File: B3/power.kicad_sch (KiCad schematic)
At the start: 31 parts, among them U301 74HC04, U302 74HC125, U303 74HC74, U304 74HC74, U305 74HC74, U306 74HC32, U309 74HC00, U314 74HC32, U316 74HC00, U317 74HC74, U318 74HC08, U319 74HC32

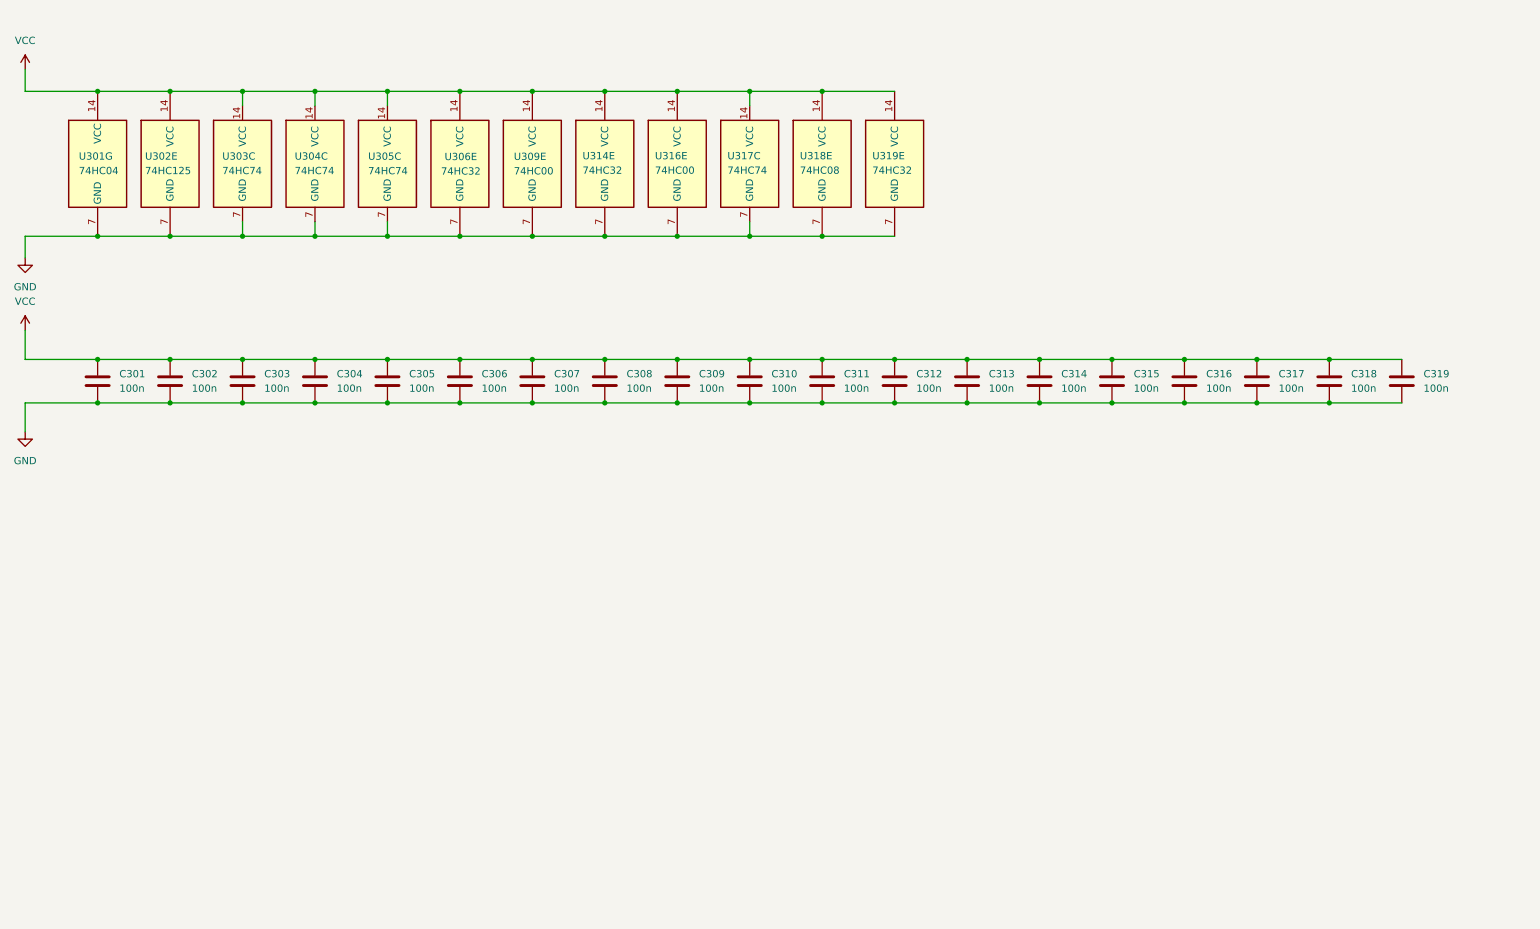
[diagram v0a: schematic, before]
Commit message: B3 added. First revision
Still not verified.
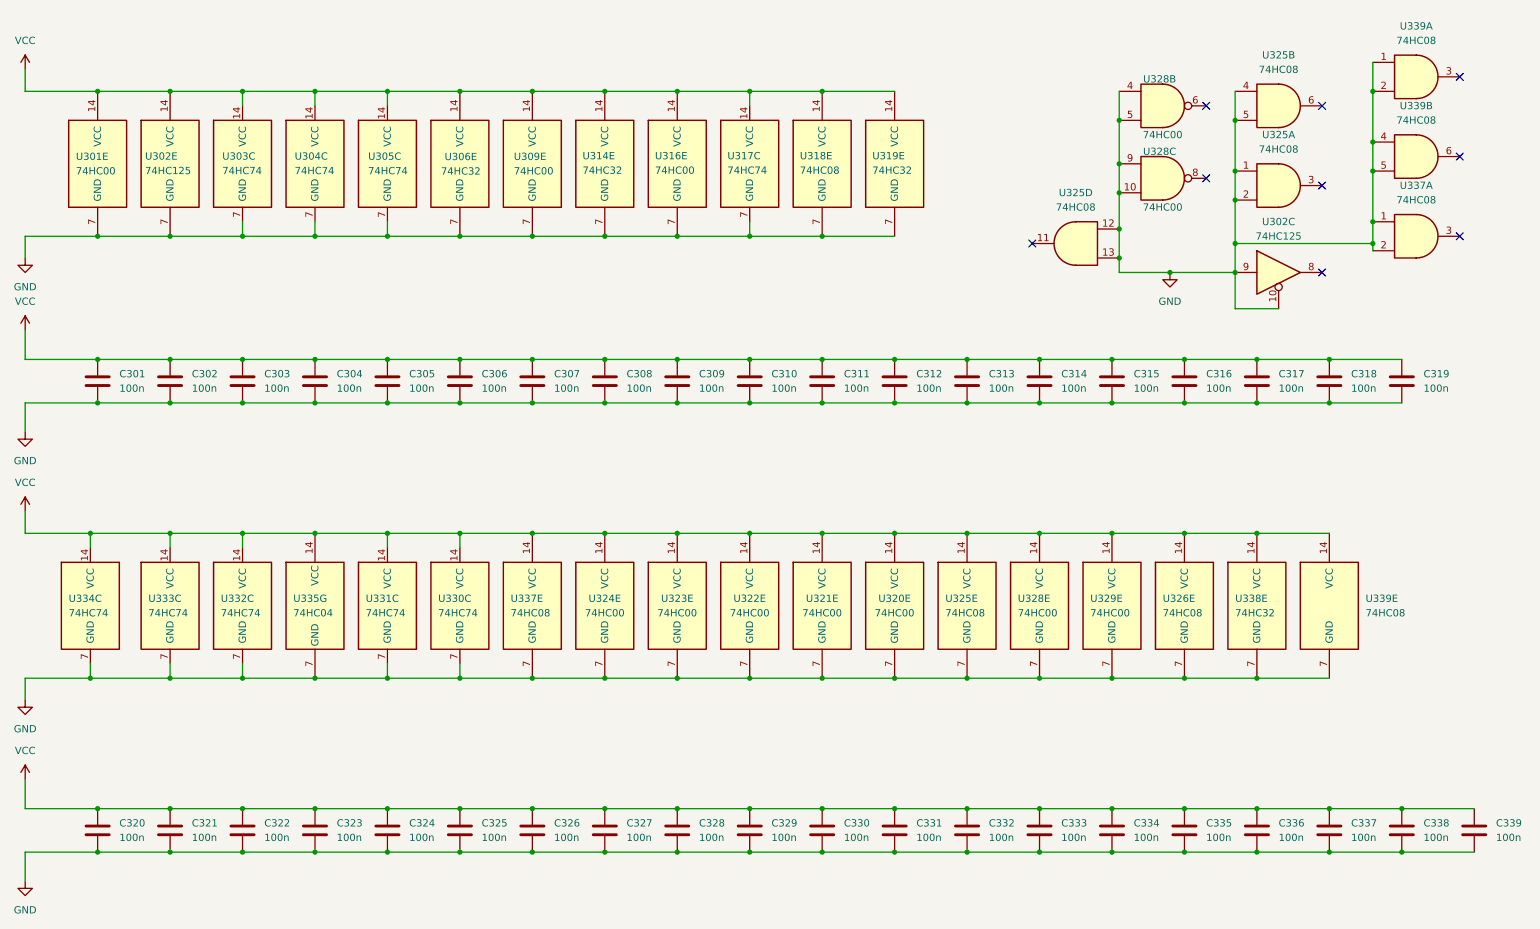
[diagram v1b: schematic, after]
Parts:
- removed U301: 74HC04, Package_SO:SO-14_3.9x8.65mm_P1.27mm, symbol 74xx:74HC04
- added C320, C321, C322, C323, C324, C325, C326, C327, C328, C329, C330, C331, C332, C333, C334, C335, C336, C337, C338, C339: 100n, Capacitor_SMD:C_0603_1608Metric, symbol Device:C
- added U301, U320, U321, U322, U323, U324, U328, U329: 74HC00, Package_SO:SO-14_3.9x8.65mm_P1.27mm, symbol 74xx:74HC00
- added unit 3 of U302
- added U325, U326, U337, U339: 74HC08, Package_SO:SO-14_3.9x8.65mm_P1.27mm, symbol Custom 74xx:74HC08
- added U330, U331, U332, U333, U334: 74HC74, Package_SO:SO-14_3.9x8.65mm_P1.27mm, symbol 74xx:74HC74
- added U335: 74HC04, Package_SO:SO-14_3.9x8.65mm_P1.27mm, symbol 74xx:74HC04
- added U338: 74HC32, Package_SO:SO-14_3.9x8.65mm_P1.27mm, symbol 74xx:74LS32
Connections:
- net GND: now also C320.2, C321.2, C322.2, C323.2, C324.2, C325.2, C326.2, C327.2, C328.2, C329.2, C330.2, C331.2, C332.2, C333.2, C334.2, C335.2, C336.2, C337.2, C338.2, C339.2, U301.7 (GND), U302.10, U302.9, U320.7 (GND), U321.7 (GND), U322.7 (GND), U323.7 (GND), U324.7 (GND), U325.1, U325.12, U325.13, U325.2, U325.4, U325.5, U325.7 (GND), U326.7 (GND), U328.10, U328.4, U328.5, U328.7 (GND), U328.9, U329.7 (GND), U330.7 (GND), U331.7 (GND), U332.7 (GND), U333.7 (GND), U334.7 (GND), U335.7 (GND), U337.1, U337.2, U337.7 (GND), U338.7 (GND), U339.1, U339.2, U339.4, U339.5, U339.7 (GND)
- net VCC: now also C320.1, C321.1, C322.1, C323.1, C324.1, C325.1, C326.1, C327.1, C328.1, C329.1, C330.1, C331.1, C332.1, C333.1, C334.1, C335.1, C336.1, C337.1, C338.1, C339.1, U301.14 (VCC), U320.14 (VCC), U321.14 (VCC), U322.14 (VCC), U323.14 (VCC), U324.14 (VCC), U325.14 (VCC), U326.14 (VCC), U328.14 (VCC), U329.14 (VCC), U330.14 (VCC), U331.14 (VCC), U332.14 (VCC), U333.14 (VCC), U334.14 (VCC), U335.14 (VCC), U337.14 (VCC), U338.14 (VCC), U339.14 (VCC)
- no-connect marks 0 -> 9

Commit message: .
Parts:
- removed unit 1 of U325
- removed unit 3 of U328
- added unit 3 of U309
- added unit 4 of U316
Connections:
- net GND: now also U309.10, U309.9, U316.12, U316.13
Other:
- company: (none) -> Daniel Molina
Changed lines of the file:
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@@
   (title_block
     (title "74HCT6526 Board 3")
-    (date "2022-09-11")
-    (rev "0.1")
+    (date "2022-10-08")
+    (rev "0.1.2")
+    (company "Daniel Molina")
+    (comment 1 "https://github.com/dmolinagarcia/74HCT6526")
   )
   (junction (at 160.02 152.4) (diameter 0) (color 0 0 0 0)
@@
   (junction (at 96.52 52.07) (diameter 0) (color 0 0 0 0)
   )
-  (junction (at 232.41 45.72) (diameter 0) (color 0 0 0 0)
-  )
   (junction (at 256.54 40.64) (diameter 0) (color 0 0 0 0)
   )
@@
   (junction (at 185.42 73.66) (diameter 0) (color 0 0 0 0)
   )
-  (junction (at 232.41 40.64) (diameter 0) (color 0 0 0 0)
-  )
   (junction (at 83.82 52.07) (diameter 0) (color 0 0 0 0)
   )
@@
   (junction (at 223.52 81.28) (diameter 0) (color 0 0 0 0)
   )
-  (junction (at 212.09 39.37) (diameter 0) (color 0 0 0 0)
-  )
   (junction (at 134.62 152.4) (diameter 0) (color 0 0 0 0)
   )
@@
   (junction (at 121.92 73.66) (diameter 0) (color 0 0 0 0)
   )
+  (junction (at 232.41 39.37) (diameter 0) (color 0 0 0 0)
+  )
   (junction (at 198.12 129.54) (diameter 0) (color 0 0 0 0)
   )
@@
   (junction (at 121.92 152.4) (diameter 0) (color 0 0 0 0)
   )
+  (junction (at 212.09 42.545) (diameter 0) (color 0 0 0 0)
+  )
   (junction (at 121.92 81.28) (diameter 0) (color 0 0 0 0)
   )
@@
   (junction (at 71.12 26.67) (diameter 0) (color 0 0 0 0)
   )
-  (junction (at 212.09 44.45) (diameter 0) (color 0 0 0 0)
-  )
   (junction (at 58.42 81.28) (diameter 0) (color 0 0 0 0)
   )
@@
   (junction (at 160.02 104.14) (diameter 0) (color 0 0 0 0)
   )
+  (junction (at 232.41 44.45) (diameter 0) (color 0 0 0 0)
+  )
   (junction (at 185.42 104.14) (diameter 0) (color 0 0 0 0)
   )
@@
   )
   (junction (at 185.42 160.02) (diameter 0) (color 0 0 0 0)
+  )
+  (junction (at 212.09 47.625) (diameter 0) (color 0 0 0 0)
   )
   (junction (at 160.02 52.07) (diameter 0) (color 0 0 0 0)
@@
   (no_connect (at 247.65 58.42))
   (no_connect (at 247.65 29.21))
-  (no_connect (at 227.33 41.91))
+  (no_connect (at 247.65 41.91))
+  (no_connect (at 227.33 45.085))
   (no_connect (at 196.85 53.34))
   (no_connect (at 227.33 29.21))
-  (no_connect (at 247.65 43.18))
   (no_connect (at 271.78 52.07))
   (no_connect (at 271.78 38.1))
@@
     (stroke (width 0) (type default) (color 0 0 0 0))
   )
-  (wire (pts (xy 212.09 31.75) (xy 212.09 39.37))
-    (stroke (width 0) (type default) (color 0 0 0 0))
-  )
   (wire (pts (xy 160.02 52.07) (xy 172.72 52.07))
     (stroke (width 0) (type default) (color 0 0 0 0))
@@
     (stroke (width 0) (type default) (color 0 0 0 0))
   )
+  (wire (pts (xy 212.09 31.75) (xy 212.09 42.545))
+    (stroke (width 0) (type default) (color 0 0 0 0))
+  )
   (wire (pts (xy 109.22 104.14) (xy 121.92 104.14))
     (stroke (width 0) (type default) (color 0 0 0 0))
@@
     (stroke (width 0) (type default) (color 0 0 0 0))
   )
+  (wire (pts (xy 232.41 39.37) (xy 232.41 44.45))
+    (stroke (width 0) (type default) (color 0 0 0 0))
+  )
   (wire (pts (xy 134.62 73.66) (xy 147.32 73.66))
     (stroke (width 0) (type default) (color 0 0 0 0))
@@
     (stroke (width 0) (type default) (color 0 0 0 0))
   )
+  (wire (pts (xy 232.41 44.45) (xy 232.41 53.34))
+    (stroke (width 0) (type default) (color 0 0 0 0))
+  )
   (wire (pts (xy 232.41 53.34) (xy 256.54 53.34))
     (stroke (width 0) (type default) (color 0 0 0 0))
@@
     (stroke (width 0) (type default) (color 0 0 0 0))
   )
-  (wire (pts (xy 232.41 31.75) (xy 232.41 40.64))
-    (stroke (width 0) (type default) (color 0 0 0 0))
-  )
   (wire (pts (xy 147.32 26.67) (xy 147.32 29.21))
     (stroke (width 0) (type default) (color 0 0 0 0))
@@
     (stroke (width 0) (type default) (color 0 0 0 0))
   )
-  (wire (pts (xy 212.09 39.37) (xy 212.09 44.45))
-    (stroke (width 0) (type default) (color 0 0 0 0))
-  )
   (wire (pts (xy 185.42 104.14) (xy 198.12 104.14))
     (stroke (width 0) (type default) (color 0 0 0 0))
   )
-  (wire (pts (xy 232.41 40.64) (xy 232.41 45.72))
-    (stroke (width 0) (type default) (color 0 0 0 0))
-  )
   (wire (pts (xy 212.09 55.88) (xy 212.09 58.42))
     (stroke (width 0) (type default) (color 0 0 0 0))
@@
     (stroke (width 0) (type default) (color 0 0 0 0))
   )
-  (wire (pts (xy 232.41 45.72) (xy 232.41 53.34))
+  (wire (pts (xy 232.41 31.75) (xy 232.41 39.37))
     (stroke (width 0) (type default) (color 0 0 0 0))
   )
@@
     (stroke (width 0) (type default) (color 0 0 0 0))
   )
+  (wire (pts (xy 212.09 47.625) (xy 212.09 50.8))
+    (stroke (width 0) (type default) (color 0 0 0 0))
+  )
   (wire (pts (xy 109.22 160.02) (xy 121.92 160.02))
     (stroke (width 0) (type default) (color 0 0 0 0))
@@
     (stroke (width 0) (type default) (color 0 0 0 0))
   )
+  (wire (pts (xy 212.09 42.545) (xy 212.09 47.625))
+    (stroke (width 0) (type default) (color 0 0 0 0))
+  )
   (wire (pts (xy 58.42 52.07) (xy 71.12 52.07))
     (stroke (width 0) (type default) (color 0 0 0 0))
@@
   )
   (wire (pts (xy 96.52 104.14) (xy 96.52 106.68))
-    (stroke (width 0) (type default) (color 0 0 0 0))
-  )
-  (wire (pts (xy 212.09 44.45) (xy 212.09 50.8))
     (stroke (width 0) (type default) (color 0 0 0 0))
   )
@@
     (pin "1")
     (pin "2")
-  )
-  (symbol (lib_id "Custom 74xx:74HC08") (at 240.03 43.18 0) (unit 1)
-    (in_bom yes) (on_board yes) (fields_autoplaced)
-    (property "Reference" "U325" (id 0) (at 240.03 34.29 0))
-    (property "Value" "74HC08" (id 1) (at 240.03 36.83 0))
-    (property "Footprint" "Package_SO:SO-14_3.9x8.65mm_P1.27mm" (id 2) (at 240.03 43.18 0)
-      (effects (font (size 1.27 1.27)) hide)
-    )
-    (property "Datasheet" "" (id 3) (at 240.03 36.83 0)
-      (effects (font (size 1.27 1.27)) hide)
-    )
-    (pin "1")
-    (pin "2")
-    (pin "3")
-    (pin "4")
-    (pin "5")
-    (pin "6")
-    (pin "10")
-    (pin "8")
-    (pin "9")
-    (pin "11")
-    (pin "12")
-    (pin "13")
-    (pin "14")
-    (pin "7")
   )
   (symbol (lib_id "power:VCC") (at 20.32 100.33 0) (unit 1)
@@
     (pin "7")
   )
-  (symbol (lib_id "74xx:74HC00") (at 219.71 41.91 0) (unit 3)
-    (in_bom yes) (on_board yes)
-    (property "Reference" "U328" (id 0) (at 219.17 37.2283 0))
-    (property "Value" "74HC00" (id 1) (at 219.71 46.99 0))
-    (property "Footprint" "Package_SO:SO-14_3.9x8.65mm_P1.27mm" (id 2) (at 219.71 41.91 0)
-      (effects (font (size 1.27 1.27)) hide)
-    )
-    (property "Datasheet" "http://www.ti.com/lit/gpn/sn74hc00" (id 3) (at 219.71 41.91 0)
-      (effects (font (size 1.27 1.27)) hide)
-    )
-    (pin "1")
-    (pin "2")
-    (pin "3")
-    (pin "4")
-    (pin "5")
-    (pin "6")
-    (pin "10")
-    (pin "8")
-    (pin "9")
-    (pin "11")
-    (pin "12")
-    (pin "13")
-    (pin "14")
-    (pin "7")
-  )
   (symbol (lib_id "74xx:74HC00") (at 172.72 116.84 0) (unit 5)
     (in_bom yes) (on_board yes)
@@
     (pin "7")
   )
+  (symbol (lib_id "74xx:74HC00") (at 240.03 41.91 0) (unit 3)
+    (in_bom yes) (on_board yes) (fields_autoplaced)
+    (property "Reference" "U309" (id 0) (at 240.03 33.02 0))
+    (property "Value" "74HC00" (id 1) (at 240.03 35.56 0))
+    (property "Footprint" "Package_SO:SO-14_3.9x8.65mm_P1.27mm" (id 2) (at 240.03 41.91 0)
+      (effects (font (size 1.27 1.27)) hide)
+    )
+    (property "Datasheet" "http://www.ti.com/lit/gpn/sn74hc00" (id 3) (at 240.03 41.91 0)
+      (effects (font (size 1.27 1.27)) hide)
+    )
+    (pin "1")
+    (pin "2")
+    (pin "3")
+    (pin "4")
+    (pin "5")
+    (pin "6")
+    (pin "10")
+    (pin "8")
+    (pin "9")
+    (pin "11")
+    (pin "12")
+    (pin "13")
+    (pin "14")
+    (pin "7")
+  )
   (symbol (lib_id "Device:C") (at 58.42 77.47 0) (unit 1)
     (in_bom yes) (on_board yes) (fields_autoplaced)
@@
     (pin "2")
   )
+  (symbol (lib_id "74xx:74HC00") (at 219.71 45.085 0) (unit 4)
+    (in_bom yes) (on_board yes) (fields_autoplaced)
+    (property "Reference" "U316" (id 0) (at 219.71 36.195 0))
+    (property "Value" "74HC00" (id 1) (at 219.71 38.735 0))
+    (property "Footprint" "Package_SO:SO-14_3.9x8.65mm_P1.27mm" (id 2) (at 219.71 45.085 0)
+      (effects (font (size 1.27 1.27)) hide)
+    )
+    (property "Datasheet" "http://www.ti.com/lit/gpn/sn74hc00" (id 3) (at 219.71 45.085 0)
+      (effects (font (size 1.27 1.27)) hide)
+    )
+    (pin "1")
+    (pin "2")
+    (pin "3")
+    (pin "4")
+    (pin "5")
+    (pin "6")
+    (pin "10")
+    (pin "8")
+    (pin "9")
+    (pin "11")
+    (pin "12")
+    (pin "13")
+    (pin "14")
+    (pin "7")
+  )
   (symbol (lib_id "Device:C") (at 33.02 156.21 0) (unit 1)

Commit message: .
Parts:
- removed unit 4 of U316
- added unit 3 of U335
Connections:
- net GND: now also U335.5

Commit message: Release v0.1.2. Added SDR!
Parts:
- added unit 2 of U314
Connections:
- net GND: now also U314.4, U314.5
- no-connect marks 9 -> 10
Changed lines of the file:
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@@
   (junction (at 198.12 81.28) (diameter 0) (color 0 0 0 0)
   )
+  (junction (at 212.09 33.655) (diameter 0) (color 0 0 0 0)
+  )
   (junction (at 212.09 55.88) (diameter 0) (color 0 0 0 0)
   )
@@
   (junction (at 210.82 160.02) (diameter 0) (color 0 0 0 0)
   )
+  (junction (at 212.09 38.735) (diameter 0) (color 0 0 0 0)
+  )
   (junction (at 160.02 160.02) (diameter 0) (color 0 0 0 0)
   )
@@
   )
   (no_connect (at 227.33 42.545))
+  (no_connect (at 196.85 36.195))
   (no_connect (at 247.65 58.42))
   (no_connect (at 247.65 29.21))
@@
     (stroke (width 0) (type default) (color 0 0 0 0))
   )
+  (wire (pts (xy 212.09 38.735) (xy 212.09 42.545))
+    (stroke (width 0) (type default) (color 0 0 0 0))
+  )
   (wire (pts (xy 232.41 44.45) (xy 232.41 53.34))
     (stroke (width 0) (type default) (color 0 0 0 0))
@@
     (stroke (width 0) (type default) (color 0 0 0 0))
   )
+  (wire (pts (xy 212.09 33.655) (xy 212.09 38.735))
+    (stroke (width 0) (type default) (color 0 0 0 0))
+  )
   (wire (pts (xy 20.32 104.14) (xy 31.75 104.14))
     (stroke (width 0) (type default) (color 0 0 0 0))
@@
     (stroke (width 0) (type default) (color 0 0 0 0))
   )
-  (wire (pts (xy 212.09 31.75) (xy 212.09 42.545))
+  (wire (pts (xy 212.09 31.75) (xy 212.09 33.655))
     (stroke (width 0) (type default) (color 0 0 0 0))
   )
@@
     (stroke (width 0) (type default) (color 0 0 0 0))
   )
+  (symbol (lib_id "74xx:74LS32") (at 204.47 36.195 180) (unit 2)
+    (in_bom yes) (on_board yes) (fields_autoplaced)
+    (property "Reference" "U314" (id 0) (at 204.47 26.67 0))
+    (property "Value" "74HC32" (id 1) (at 204.47 29.21 0))
+    (property "Footprint" "Package_SO:SO-14_3.9x8.65mm_P1.27mm" (id 2) (at 204.47 36.195 0)
+      (effects (font (size 1.27 1.27)) hide)
+    )
+    (property "Datasheet" "http://www.ti.com/lit/gpn/sn74LS32" (id 3) (at 204.47 36.195 0)
+      (effects (font (size 1.27 1.27)) hide)
+    )
+    (pin "1")
+    (pin "2")
+    (pin "3")
+    (pin "4")
+    (pin "5")
+    (pin "6")
+    (pin "10")
+    (pin "8")
+    (pin "9")
+    (pin "11")
+    (pin "12")
+    (pin "13")
+    (pin "14")
+    (pin "7")
+  )
   (symbol (lib_id "power:GND") (at 220.98 58.42 0) (unit 1)

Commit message: B0 ready for v0.2.0 release.
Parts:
- added C340: 100n, Capacitor_SMD:C_0603_1608Metric, symbol Device:C
- added U340: 74HC74, symbol 74xx:74HC74
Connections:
- net GND: now also C340.2, U340.7 (GND)
- net VCC: now also C340.1, U340.10 (~{S}), U340.11 (C), U340.12 (D), U340.13 (~{R}), U340.14 (VCC)
- no-connect marks 10 -> 12
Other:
- moved on the sheet: C320, C321, C322, C323, C324, C325, C326, C327, C328, C329, C330, C331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

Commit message: B3 ready for v0.2.0 release
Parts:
- U340: footprint (none) -> Package_SO:SO-14_3.9x8.65mm_P1.27mm
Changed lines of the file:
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@@
       (effects (font (size 1.27 1.27)) (justify left))
     )
-    (property "Footprint" "" (id 2) (at 266.7 63.5 0)
+    (property "Footprint" "Package_SO:SO-14_3.9x8.65mm_P1.27mm" (id 2) (at 266.7 63.5 0)
       (effects (font (size 1.27 1.27)) hide)
     )
@@
       (effects (font (size 1.27 1.27)) (justify left))
     )
-    (property "Footprint" "" (id 2) (at 261.62 116.84 0)
-      (effects (font (size 1.27 1.27)) hide)
-    )
+    (property "Footprint" "Package_SO:SO-14_3.9x8.65mm_P1.27mm" (id 2) (at 261.62 116.84 0)
+      (effects (font (size 1.27 1.27)) hide)
+    )

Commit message: .
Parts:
- U302: value 74HC125 -> 74HCT125
- U305: value 74HC74 -> 74HCT74
- U335: value 74HC04 -> 74HCT04
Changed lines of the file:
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@@
     (in_bom yes) (on_board yes) (fields_autoplaced)
     (property "Reference" "U302" (id 0) (at 233.68 48.26 0))
-    (property "Value" "74HC125" (id 1) (at 233.68 50.8 0))
+    (property "Value" "74HCT125" (id 1) (at 233.68 50.8 0))
     (property "Footprint" "Package_SO:SO-14_3.9x8.65mm_P1.27mm" (id 2) (at 233.68 57.15 0)
       (effects (font (size 1.27 1.27)) hide)
@@
       (effects (font (size 1.27 1.27)) (justify left))
     )
-    (property "Value" "74HC125" (id 1) (at 41.3315 40.5919 0)
+    (property "Value" "74HCT125" (id 1) (at 41.3315 40.5919 0)
       (effects (font (size 1.27 1.27)) (justify left))
     )
@@
     (in_bom yes) (on_board yes)
     (property "Reference" "U335" (id 0) (at 217.17 36.195 0))
-    (property "Value" "74HC04" (id 1) (at 217.17 38.735 0))
+    (property "Value" "74HCT04" (id 1) (at 217.17 38.735 0))
     (property "Footprint" "Package_SO:SO-14_3.9x8.65mm_P1.27mm" (id 2) (at 213.36 41.275 0)
       (effects (font (size 1.27 1.27)) hide)
@@
       (effects (font (size 1.27 1.27)) (justify left))
     )
-    (property "Value" "74HC74" (id 1) (at 80.4333 40.6136 0)
+    (property "Value" "74HCT74" (id 1) (at 80.4333 40.6136 0)
       (effects (font (size 1.27 1.27)) (justify left))
     )
@@
       (effects (font (size 1.27 1.27)) (justify left))
     )
-    (property "Value" "74HC04" (id 1) (at 67.31 118.11 0)
-      (effects (font (size 1.27 1.27)) (justify left))
-    )
+    (property "Value" "74HCT04" (id 1) (at 67.31 118.11 0)
+      (effects (font (size 1.27 1.27)) (justify left))
+    )
